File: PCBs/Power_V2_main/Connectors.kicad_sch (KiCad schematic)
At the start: 1 part, among them J4 PCIE-164-02-F-D-TH-TR

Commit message: shortened main board and secondary
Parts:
- J4: footprint IPRL_footprints:SAMTEC_PCIE-164-02-F-D-TH-TR -> iprl_footprints:SAMTEC_PCIE-164-02-F-D-TH-TR
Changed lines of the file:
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@@
 			)
 		)
-		(property "Footprint" "IPRL_footprints:SAMTEC_PCIE-164-02-F-D-TH-TR"
+		(property "Footprint" "iprl_footprints:SAMTEC_PCIE-164-02-F-D-TH-TR"
 			(at 189.23 97.79 0)
 			(effects
@@
 			)
 		)
-		(property "Footprint" "IPRL_footprints:SAMTEC_PCIE-164-02-F-D-TH-TR"
+		(property "Footprint" "iprl_footprints:SAMTEC_PCIE-164-02-F-D-TH-TR"
 			(at 129.54 97.79 0)
 			(effects

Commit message: main schematic for power board main
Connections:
- net OUT_READ: no longer J4.A1
- new net PLUGGED_IN: J4.A1
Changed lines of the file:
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@@
-	)
-	(junction
-		(at 116.84 49.53)
-		(diameter 0)
-		(color 0 0 0 0)
 	)
 	(junction
@@
 	(wire
 		(pts
+			(xy 113.03 46.99) (xy 116.84 46.99)
+		)
+		(stroke
+			(width 0)
+			(type default)
+		)
+	)
+	(wire
+		(pts
 			(xy 201.93 97.79) (xy 201.93 100.33)
 		)
@@
 	(wire
 		(pts
+			(xy 35.56 181.61) (xy 41.91 181.61)
+		)
+		(stroke
+			(width 0)
+			(type default)
+		)
+	)
+	(wire
+		(pts
 			(xy 201.93 130.81) (xy 201.93 133.35)
 		)
@@
 		(pts
 			(xy 116.84 95.25) (xy 116.84 97.79)
-		)
-		(stroke
-			(width 0)
-			(type default)
-		)
-	)
-	(wire
-		(pts
-			(xy 116.84 46.99) (xy 116.84 49.53)
 		)
 		(stroke
@@
 		)
 	)
+	(label "PLUGGED_IN"
+		(at 35.56 181.61 180)
+		(effects
+			(font
+				(size 1.27 1.27)
+			)
+			(justify right bottom)
+		)
+	)
 	(label "OUT_READ"
 		(at 107.95 72.39 180)
@@
 		)
 	)
+	(label "PLUGGED_IN"
+		(at 113.03 46.99 180)
+		(effects
+			(font
+				(size 1.27 1.27)
+			)
+			(justify right bottom)
+		)
+	)
 	(label "14V8_OUT"
 		(at 109.22 148.59 180)
@@
 		(effects
 			(font
+				(size 1.27 1.27)
+			)
+			(justify left)
+		)
+	)
+	(hierarchical_label "PLUGGED_IN"
+		(shape input)
+		(at 41.91 181.61 0)
+		(effects
+			(font

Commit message: a 5 hour binge of PCB layout on the main
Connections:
- net PLUGGED_IN is gone; now on net OUT_READ: J4.A1

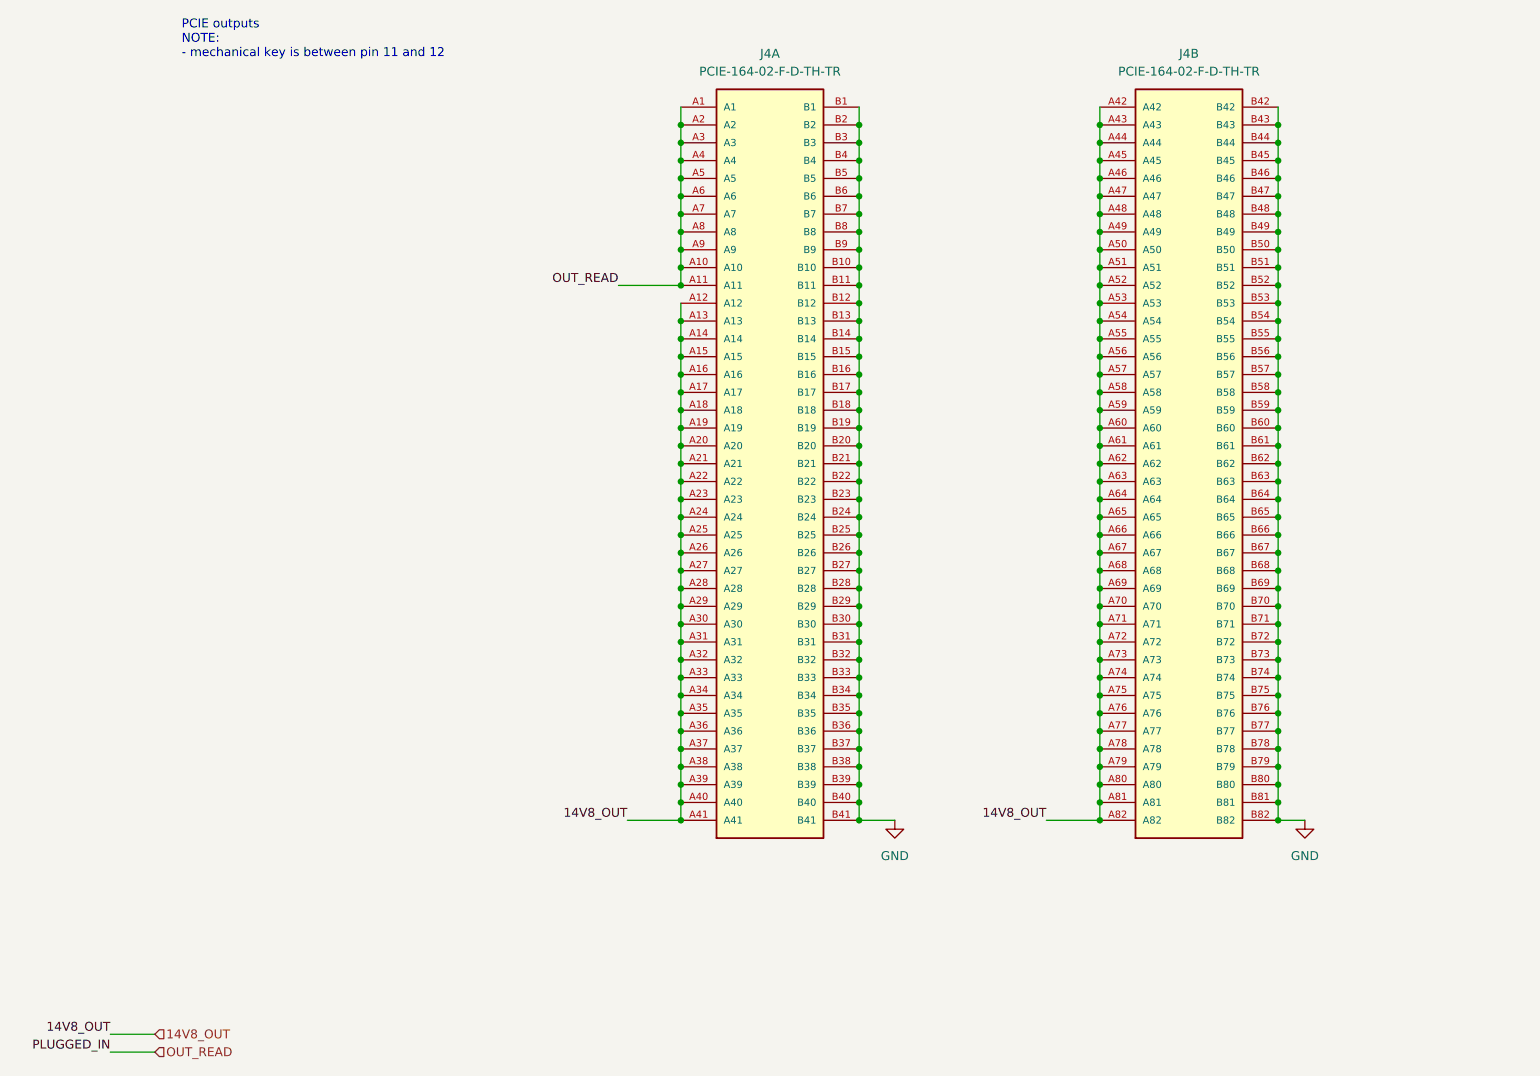
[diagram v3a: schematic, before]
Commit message: added LED indicators to board and redid power distribution in PCIe
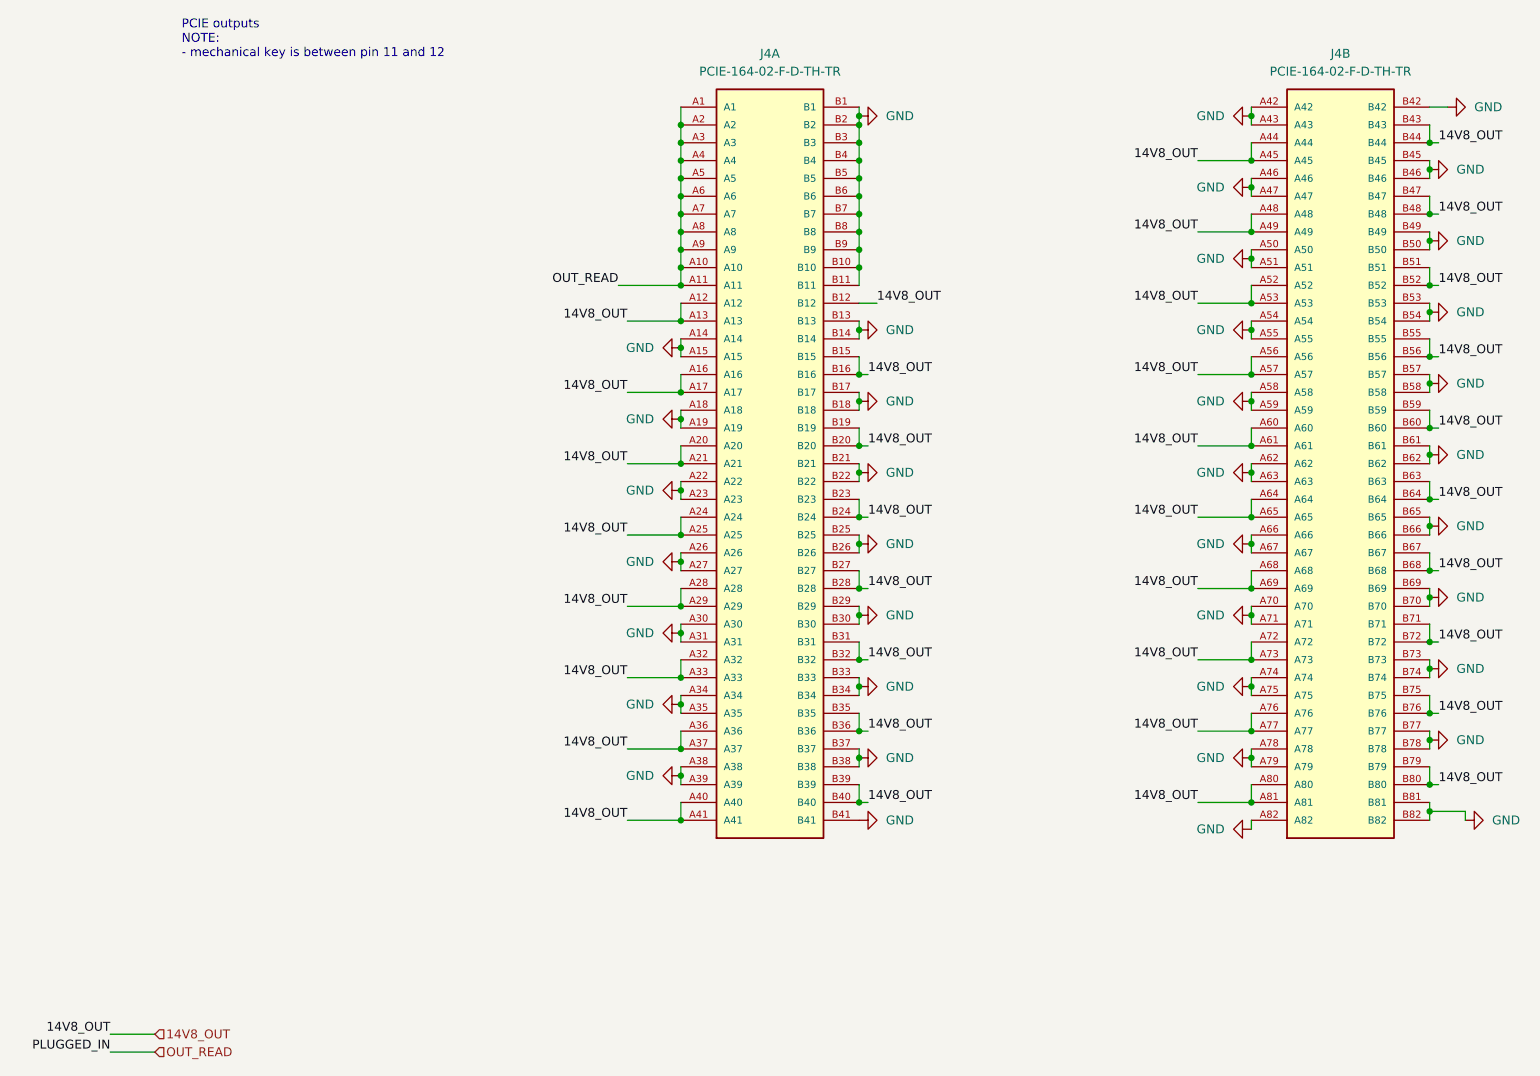
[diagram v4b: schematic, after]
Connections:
- net 14V8_OUT: now also J4.B12, J4.B15, J4.B16, J4.B19, J4.B20, J4.B23, J4.B24, J4.B27, J4.B28, J4.B31, J4.B32, J4.B35, J4.B36, J4.B39, J4.B40, J4.B43, J4.B44, J4.B47, J4.B48, J4.B51, J4.B52, J4.B55, J4.B56, J4.B59, J4.B60, J4.B63, J4.B64, J4.B67, J4.B68, J4.B71, J4.B72, J4.B75, J4.B76, J4.B79, J4.B80; no longer J4.A14, J4.A15, J4.A18, J4.A19, J4.A22, J4.A23, J4.A26, J4.A27, J4.A30, J4.A31, J4.A34, J4.A35, J4.A38, J4.A39, J4.A42, J4.A43, J4.A46, J4.A47, J4.A50, J4.A51, J4.A54, J4.A55, J4.A58, J4.A59, J4.A62, J4.A63, J4.A66, J4.A67, J4.A70, J4.A71, J4.A74, J4.A75, J4.A78, J4.A79, J4.A82
- net GND: now also J4.A14, J4.A15, J4.A18, J4.A19, J4.A22, J4.A23, J4.A26, J4.A27, J4.A30, J4.A31, J4.A34, J4.A35, J4.A38, J4.A39, J4.A42, J4.A43, J4.A46, J4.A47, J4.A50, J4.A51, J4.A54, J4.A55, J4.A58, J4.A59, J4.A62, J4.A63, J4.A66, J4.A67, J4.A70, J4.A71, J4.A74, J4.A75, J4.A78, J4.A79, J4.A82; no longer J4.B12, J4.B15, J4.B16, J4.B19, J4.B20, J4.B23, J4.B24, J4.B27, J4.B28, J4.B31, J4.B32, J4.B35, J4.B36, J4.B39, J4.B40, J4.B43, J4.B44, J4.B47, J4.B48, J4.B51, J4.B52, J4.B55, J4.B56, J4.B59, J4.B60, J4.B63, J4.B64, J4.B67, J4.B68, J4.B71, J4.B72, J4.B75, J4.B76, J4.B79, J4.B80
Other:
- moved on the sheet: J4B
